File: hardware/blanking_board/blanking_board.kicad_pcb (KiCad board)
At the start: 2 copper layers, 95 x 82 mm, 22 parts, among them J1 B4B-XH-A_LF__SN_, J10 Conn_01x02_Female, J11 DB25_Female_MountingHoles, J12 DB25_Female_MountingHoles, J2 B4B-XH-A_LF__SN_, J3 B4B-XH-A_LF__SN_, J4 B2B-XH-A_LF__SN_, J5 B4B-XH-A_LF__SN_, J6 B4B-XH-A_LF__SN_, J7 B4B-XH-A_LF__SN_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

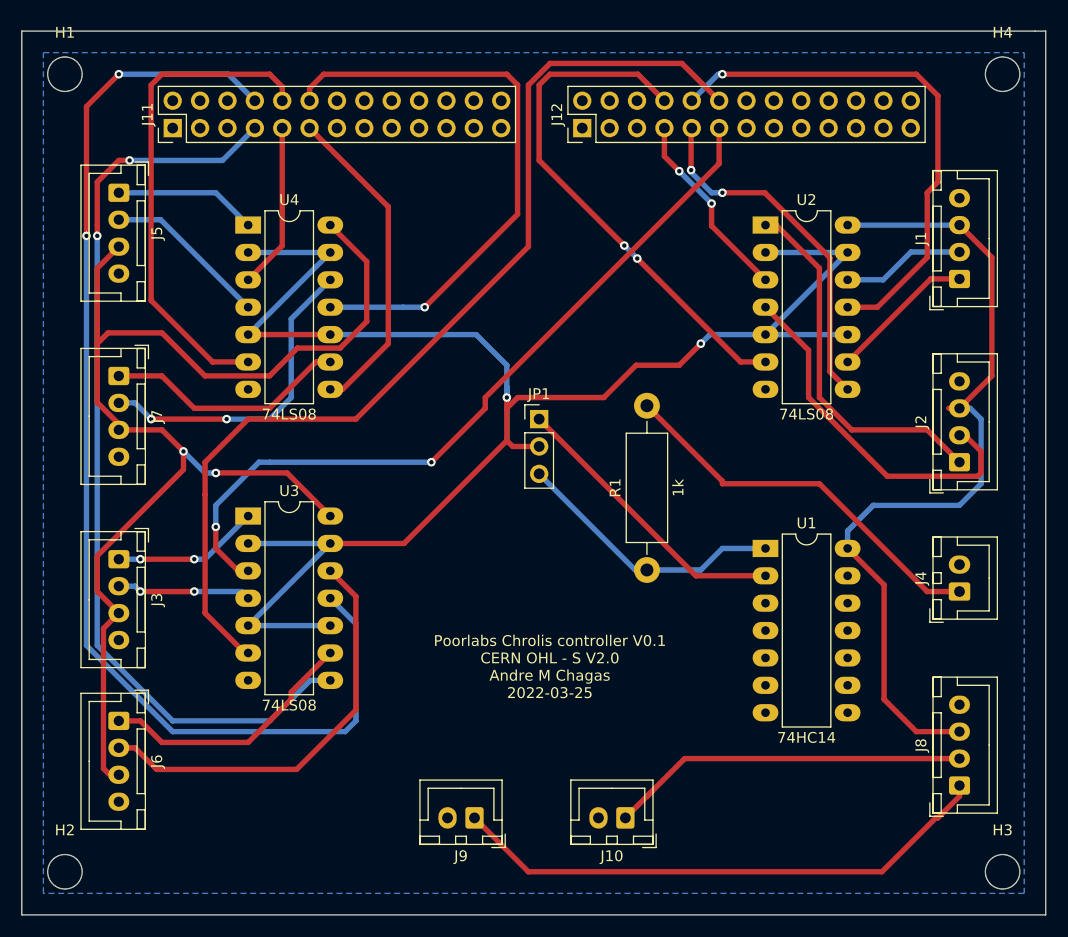
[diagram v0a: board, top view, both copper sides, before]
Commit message: update pcb with jumper for no blanking
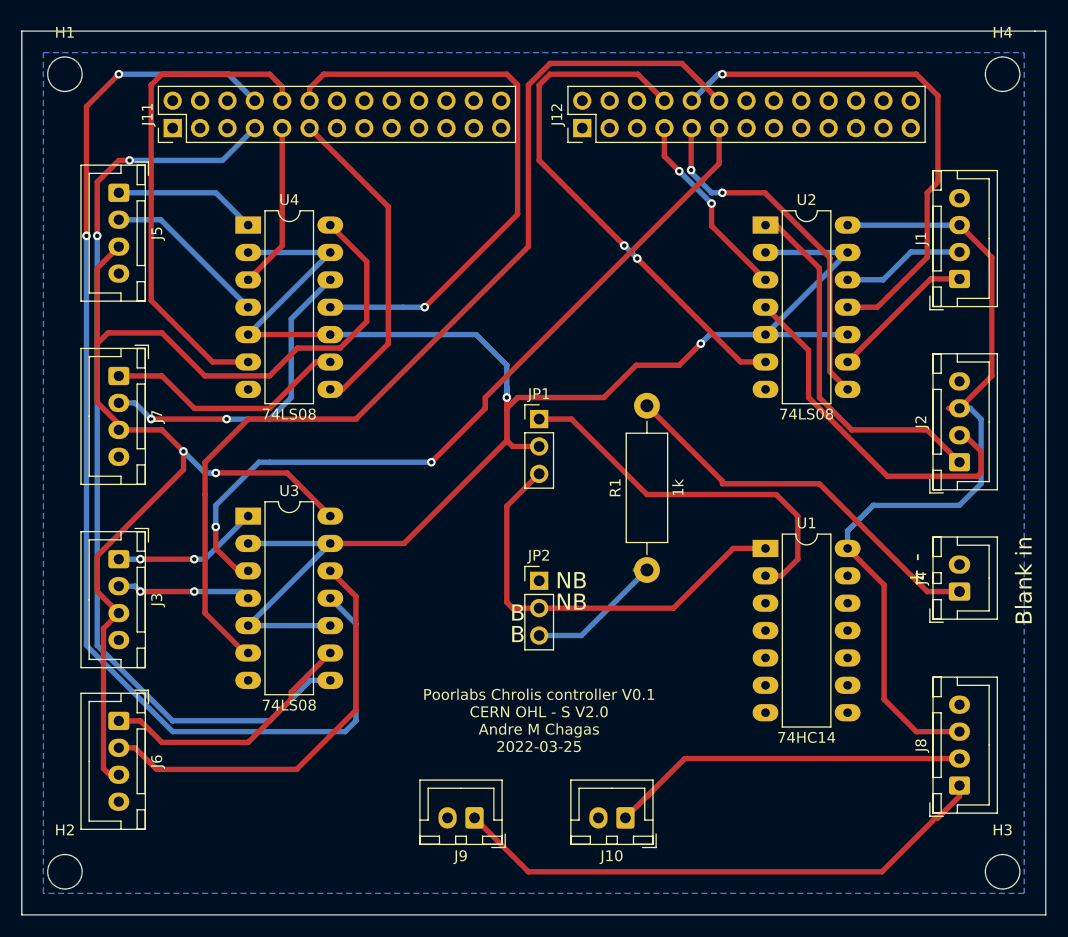
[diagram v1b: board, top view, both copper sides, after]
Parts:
- added JP2: Jumper_NC_Dual, Connector_PinHeader_2.54mm:PinHeader_1x03_P2.54mm_Vertical, F.Cu at (146.0, 98.0)
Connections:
- J11 pad 1: Net-(J11-Pad1) -> unconnected-(J11-Pad1)
- J11 pad 2: Net-(J11-Pad2) -> unconnected-(J11-Pad2)
- J11 pad 3: Net-(J11-Pad3) -> unconnected-(J11-Pad3)
- J11 pad 4: Net-(J11-Pad4) -> unconnected-(J11-Pad4)
- J11 pad 5: Net-(J11-Pad5) -> unconnected-(J11-Pad5)
- J11 pad 6: Net-(J11-Pad6) -> unconnected-(J11-Pad6)
- J12 pad 1: Net-(J12-Pad1) -> unconnected-(J12-Pad1)
- J12 pad 2: Net-(J12-Pad2) -> unconnected-(J12-Pad2)
- J12 pad 3: Net-(J12-Pad3) -> unconnected-(J12-Pad3)
- J12 pad 4: Net-(J12-Pad4) -> unconnected-(J12-Pad4)
- J12 pad 5: Net-(J12-Pad5) -> unconnected-(J12-Pad5)
- J12 pad 6: Net-(J12-Pad6) -> unconnected-(J12-Pad6)
- R1 pad 1: Net-(JP1-Pad3) -> Net-(R1-Pad1)
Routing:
- net Net-(JP1-Pad3): track 25.5 -> 39.7 mm
- net Net-(R1-Pad1): track 0.00 -> 13.6 mm
- net Net-(JP1-Pad1): track 27.0 -> 35.4 mm
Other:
- net class Default removed
- board text added: "+ -"
- board text added: "B"
- board text added: "Blank in"
- board text added: "NB"

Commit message: more details on board
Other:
- board text added: "I"
- board text added: "NI"
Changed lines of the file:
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@@
     (effects (font (size 1.5 1.5) (thickness 0.3)))
+  )
+  (gr_text "NI\n" (at 148.75 88) (layer "F.SilkS")
+    (effects (font (size 1 1) (thickness 0.15)))
+  )
+  (gr_text "I\n" (at 148.25 83) (layer "F.SilkS")
+    (effects (font (size 1 1) (thickness 0.15)))
   )
   (gr_text "Poorlabs Chrolis controller V0.1\nCERN OHL - S V2.0\nAndre M Chagas\n2022-03-25" (at 146 111) (layer "F.SilkS")
@@
     (effects (font (size 1.5 1.5) (thickness 0.3)))
   )
+  (dimension (type aligned) (layer "Eco2.User")
+    (pts (xy 195 47) (xy 195 129))
+    (height -11)
+    (gr_text "82.0000 mm" (at 204.85 88 90) (layer "Eco2.User")
+      (effects (font (size 1 1) (thickness 0.15)))
+    )
+    (format (units 3) (units_format 1) (precision 4))
+    (style (thickness 0.1) (arrow_length 1.27) (text_position_mode 0) (extension_height 0.58642) (extension_offset 0.5) keep_text_aligned)
+  )
+  (dimension (type aligned) (layer "Eco2.User")
+    (pts (xy 98 135) (xy 193 135))
+    (height 17)
+    (gr_text "95.0000 mm" (at 145.5 150.85) (layer "Eco2.User")
+      (effects (font (size 1 1) (thickness 0.15)))
+    )
+    (format (units 3) (units_format 1) (precision 4))
+    (style (thickness 0.1) (arrow_length 1.27) (text_position_mode 0) (extension_height 0.58642) (extension_offset 0.5) keep_text_aligned)
+  )
   (target plus (at 102 125) (size 5) (width 0.05) (layer "Edge.Cuts"))

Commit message: update board details
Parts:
- moved H3 0.33 mm to (188.7, 125.1)
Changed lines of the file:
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@@
   )
   (footprint "MountingHole:MountingHole_3.2mm_M3_ISO7380" (layer "F.Cu")
-    (at 189 125)
+    (at 188.678 125.063)
     (descr "Mounting Hole 3.2mm, no annular, M3, ISO7380")
     (tags "mounting hole 3.2mm no annular m3 iso7380")
@@
       (effects (font (size 1 1) (thickness 0.15)))
     )
-    (fp_text user "${REFERENCE}" (at 0.3 0) (layer "F.Fab")
+    (fp_text user "${REFERENCE}" (at 0.254 0.19) (layer "F.Fab")
       (effects (font (size 1 1) (thickness 0.15)))
     )
@@
       )
     )
+  )
+  (zone (net 0) (net_name "") (layer "B.Cu") (hatch edge 0.508)
+    (connect_pads (clearance 0))
+    (min_thickness 0.254)
+    (keepout (tracks not_allowed) (vias not_allowed) (pads not_allowed ) (copperpour not_allowed) (footprints allowed))
+    (fill (thermal_gap 0.508) (thermal_bridge_width 0.508))
+    (polygon
+      (pts
+        (xy 104.35 53.054)
+        (xy 98.127 53.054)
+        (xy 98.127 47.212)
+        (xy 104.35 47.212)
+      )
+    )
+  )
+  (zone (net 0) (net_name "") (layer "B.Cu") (hatch edge 0.508)
+    (connect_pads (clearance 0))
+    (min_thickness 0.254)
+    (keepout (tracks not_allowed) (vias not_allowed) (pads not_allowed ) (copperpour not_allowed) (footprints allowed))
+    (fill (thermal_gap 0.508) (thermal_bridge_width 0.508))
+    (polygon
+      (pts
+        (xy 190.964 126.968)
+        (xy 184.741 126.968)
+        (xy 184.741 121.126)
+        (xy 190.964 121.126)
+      )
+    )
+  )
+  (zone (net 0) (net_name "") (layer "B.Cu") (hatch edge 0.508)
+    (connect_pads (clearance 0))
+    (min_thickness 0.254)
+    (keepout (tracks not_allowed) (vias not_allowed) (pads not_allowed ) (copperpour not_allowed) (footprints allowed))
+    (fill (thermal_gap 0.508) (thermal_bridge_width 0.508))
+    (polygon
+      (pts
+        (xy 190.964 54.832)
+        (xy 184.741 54.832)
+        (xy 184.741 48.99)
+        (xy 190.964 48.99)
+      )
+    )
+  )
+  (zone (net 0) (net_name "") (layer "B.Cu") (hatch edge 0.508)
+    (connect_pads (clearance 0))
+    (min_thickness 0.254)
+    (keepout (tracks not_allowed) (vias not_allowed) (pads not_allowed ) (copperpour not_allowed) (footprints allowed))
+    (fill (thermal_gap 0.508) (thermal_bridge_width 0.508))
+    (polygon
+      (pts
+        (xy 106.128 126.968)
+        (xy 99.905 126.968)
+        (xy 99.905 121.126)
+        (xy 106.128 121.126)
+      )
+    )
